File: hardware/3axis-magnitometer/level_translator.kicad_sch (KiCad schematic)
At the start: 10 parts, among them Q1 BSS138, Q2 BSS138

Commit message: Add files via upload
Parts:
- removed Q1, Q2: BSS138, Package_TO_SOT_SMD:SOT-23, symbol Transistor_FET:BSS138
- removed R20, R21, R24, R25: 2.2k, Resistor_SMD:R_0805_2012Metric, symbol Device:R
- removed R22, R23: 0, Resistor_SMD:R_0805_2012Metric, symbol Device:R
- added C28, C29, C30, C31, C34, C35: 0.22, Capacitor_SMD:C_0805_2012Metric, symbol Device:C
- added U10, U11: SP3485CN, Package_SO:SOIC-8_3.9x4.9mm_P1.27mm, symbol Interface_UART:SP3485CN
- added U7, U8: 74LVC2T45DC, Package_SO:VSSOP-8_2.3x2mm_P0.5mm, symbol Logic_LevelTranslator:74LVC2T45DC
- renumbered R19 to R14, R26 to R15
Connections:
- net at R15.1: now also C30.1, C31.1, C34.1, C35.1, U10.8 (VCC), U11.8 (VCC), U7.8 (VCCB), U8.8 (VCCB)
- net at R14.2: now also C28.1, C29.1, U7.1 (VCCA), U8.1 (VCCA), U8.5 (DIR)
- new net 485_1_A: U10.6 (A)
- new net 485_1_B: U10.7 (B)
- new net 485_2_A: U11.6 (A)
- new net 485_2_B: U11.7 (B)
- new net GND: C28.2, C29.2, C30.2, C31.2, C34.2, C35.2, U10.5 (GND), U11.5 (GND), U7.4 (GND), U7.5 (DIR), U8.4 (GND)
- new net RX0: U8.2 (1A)
- new net RX1: U8.3 (2A)
- new net TX0: U7.2 (1A)
- new net TX1: U7.3 (2A)
- new net UART_RX0: U10.1 (RO), U8.7 (1B)
- new net UART_RX1: U11.1 (RO), U8.6 (2B)
- new net UART_TX0: U10.4 (DI), U7.7 (1B)
- new net UART_TX1: U11.4 (DI), U7.6 (2B)
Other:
- moved on the sheet: R14, R15

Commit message: начата новая трассировка
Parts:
- added JP1, JP2, JP3, JP4: SolderJumper_2_Open, Jumper:SolderJumper-2_P1.3mm_Open_TrianglePad1.0x1.5mm, symbol Jumper:SolderJumper_2_Open
- added JP5, JP6, JP7, JP8: SolderJumper_3_Open, Jumper:SolderJumper-3_P2.0mm_Open_TrianglePad1.0x1.5mm_NumberLabels, symbol Jumper:SolderJumper_3_Open
- added R15, R16: 2.2k, Resistor_SMD:R_0805_2012Metric, symbol Device:R
- renumbered C28 to C29, C29 to C30, C30 to C32, C34 to C33, C35 to C34, R15 to R17, U11 to U10, U10 to U9
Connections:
- net RX0: now also JP2.1 (A)
- net RX1: now also JP4.1 (A)
- net TX0: now also JP1.1 (A)
- net TX1: now also JP3.1 (A)
- net UART_RX0: now also JP7.2 (C); no longer U8.7 (1B), U9.1 (RO)
- net UART_RX1: now also JP8.2 (C); no longer U10.1 (RO), U8.6 (2B)
- net UART_TX0: now also JP5.2 (C); no longer U7.7 (1B), U9.4 (DI)
- net UART_TX1: now also JP6.2 (C); no longer U10.4 (DI), U7.6 (2B)
- net at C31.1, C32.1, C33.1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: now also R15.1, R16.1
- net at U9.2 (~{RE}): now also U9.3 (DE), R15.2
- net at U10.2 (~{RE}): now also U10.3 (DE), R16.2
- new net: JP3.2 (B), JP6.3 (B), U7.6 (2B)
- new net: JP1.2 (B), JP5.3 (B), U7.7 (1B)
- new net: JP6.1 (A), U10.4 (DI)
- new net: JP7.1 (A), U9.1 (RO)
- new net: JP2.2 (B), JP7.3 (B), U8.7 (1B)
- new net: JP4.2 (B), JP8.3 (B), U8.6 (2B)
- new net: JP5.1 (A), U9.4 (DI)
- new net: JP8.1 (A), U10.1 (RO)
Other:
- moved on the sheet: C29, C30, C31, C32, C33, C34, R17, U10, U7, U8, U9

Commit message: трасировка магнитометра
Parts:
- JP1, JP2, JP3, JP4: footprint Jumper:SolderJumper-2_P1.3mm_Open_TrianglePad1.0x1.5mm -> Jumper:SolderJumper-2_P1.3mm_Open_Pad1.0x1.5mm
- JP5, JP6, JP7, JP8: footprint Jumper:SolderJumper-3_P2.0mm_Open_TrianglePad1.0x1.5mm_NumberLabels -> Jumper:SolderJumper-3_P1.3mm_Open_Pad1.0x1.5mm
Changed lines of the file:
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@@
 			)
 		)
-		(property "Footprint" "Jumper:SolderJumper-3_P2.0mm_Open_TrianglePad1.0x1.5mm_NumberLabels"
+		(property "Footprint" "Jumper:SolderJumper-3_P1.3mm_Open_Pad1.0x1.5mm"
 			(at 137.16 68.58 0)
 			(effects
@@
 			)
 		)
-		(property "Footprint" "Jumper:SolderJumper-3_P2.0mm_Open_TrianglePad1.0x1.5mm_NumberLabels"
+		(property "Footprint" "Jumper:SolderJumper-3_P1.3mm_Open_Pad1.0x1.5mm"
 			(at 144.78 92.71 0)
 			(effects
@@
 			)
 		)
-		(property "Footprint" "Jumper:SolderJumper-2_P1.3mm_Open_TrianglePad1.0x1.5mm"
+		(property "Footprint" "Jumper:SolderJumper-2_P1.3mm_Open_Pad1.0x1.5mm"
 			(at 93.98 25.4 0)
 			(effects
@@
 			)
 		)
-		(property "Footprint" "Jumper:SolderJumper-2_P1.3mm_Open_TrianglePad1.0x1.5mm"
+		(property "Footprint" "Jumper:SolderJumper-2_P1.3mm_Open_Pad1.0x1.5mm"
 			(at 93.98 63.5 0)
 			(effects
@@
 			)
 		)
-		(property "Footprint" "Jumper:SolderJumper-2_P1.3mm_Open_TrianglePad1.0x1.5mm"
+		(property "Footprint" "Jumper:SolderJumper-2_P1.3mm_Open_Pad1.0x1.5mm"
 			(at 88.9 59.69 0)
 			(effects
@@
 			)
 		)
-		(property "Footprint" "Jumper:SolderJumper-2_P1.3mm_Open_TrianglePad1.0x1.5mm"
+		(property "Footprint" "Jumper:SolderJumper-2_P1.3mm_Open_Pad1.0x1.5mm"
 			(at 88.9 21.59 0)
 			(effects
@@
 			)
 		)
-		(property "Footprint" "Jumper:SolderJumper-3_P2.0mm_Open_TrianglePad1.0x1.5mm_NumberLabels"
+		(property "Footprint" "Jumper:SolderJumper-3_P1.3mm_Open_Pad1.0x1.5mm"
 			(at 130.81 54.61 0)
 			(effects
@@
 			)
 		)
-		(property "Footprint" "Jumper:SolderJumper-3_P2.0mm_Open_TrianglePad1.0x1.5mm_NumberLabels"
+		(property "Footprint" "Jumper:SolderJumper-3_P1.3mm_Open_Pad1.0x1.5mm"
 			(at 152.4 106.68 0)
 			(effects

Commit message: Финальные правки трассировки
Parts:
- renumbered C29 to C30, C30 to C31, C31 to C32, C32 to C33, C33 to C34, C34 to C35
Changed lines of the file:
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@@
 		(on_board yes)
 		(dnp no)
-		(property "Reference" "C33"
+		(property "Reference" "C34"
 			(at 116.84 110.236 0)
 			(effects
@@
 			(project "3axis-magnitometer"
 				(path "/c590c88d-27c9-4e5a-a435-a42d9de70c1c/83e74227-fab1-47ae-b3ea-3e1f54a43bc9"
-					(reference "C33")
+					(reference "C34")
 					(unit 1)
 				)
@@
 		(on_board yes)
 		(dnp no)
-		(property "Reference" "C29"
+		(property "Reference" "C30"
 			(at 78.74 36.576 0)
 			(effects
@@
 			(project "3axis-magnitometer"
 				(path "/c590c88d-27c9-4e5a-a435-a42d9de70c1c/83e74227-fab1-47ae-b3ea-3e1f54a43bc9"
-					(reference "C29")
+					(reference "C30")
 					(unit 1)
 				)
@@
 		(on_board yes)
 		(dnp no)
-		(property "Reference" "C32"
+		(property "Reference" "C33"
 			(at 116.84 93.726 0)
 			(effects
@@
 			(project "3axis-magnitometer"
 				(path "/c590c88d-27c9-4e5a-a435-a42d9de70c1c/83e74227-fab1-47ae-b3ea-3e1f54a43bc9"
-					(reference "C32")
+					(reference "C33")
 					(unit 1)
 				)
@@
 		(on_board yes)
 		(dnp no)
-		(property "Reference" "C30"
+		(property "Reference" "C31"
 			(at 78.74 94.996 0)
 			(effects
@@
 			(project "3axis-magnitometer"
 				(path "/c590c88d-27c9-4e5a-a435-a42d9de70c1c/83e74227-fab1-47ae-b3ea-3e1f54a43bc9"
-					(reference "C30")
+					(reference "C31")
 					(unit 1)
 				)
@@
 		(on_board yes)
 		(dnp no)
-		(property "Reference" "C31"
+		(property "Reference" "C32"
 			(at 116.84 51.816 0)
 			(effects
@@
 			(project "3axis-magnitometer"
 				(path "/c590c88d-27c9-4e5a-a435-a42d9de70c1c/83e74227-fab1-47ae-b3ea-3e1f54a43bc9"
-					(reference "C31")
+					(reference "C32")
 					(unit 1)
 				)
@@
 		(on_board yes)
 		(dnp no)
-		(property "Reference" "C34"
+		(property "Reference" "C35"
 			(at 116.84 148.336 0)
 			(effects
@@
 			(project "3axis-magnitometer"
 				(path "/c590c88d-27c9-4e5a-a435-a42d9de70c1c/83e74227-fab1-47ae-b3ea-3e1f54a43bc9"
-					(reference "C34")
-					(unit 1)
-				)
+					(reference "C35")
+					(unit 1)
+				)

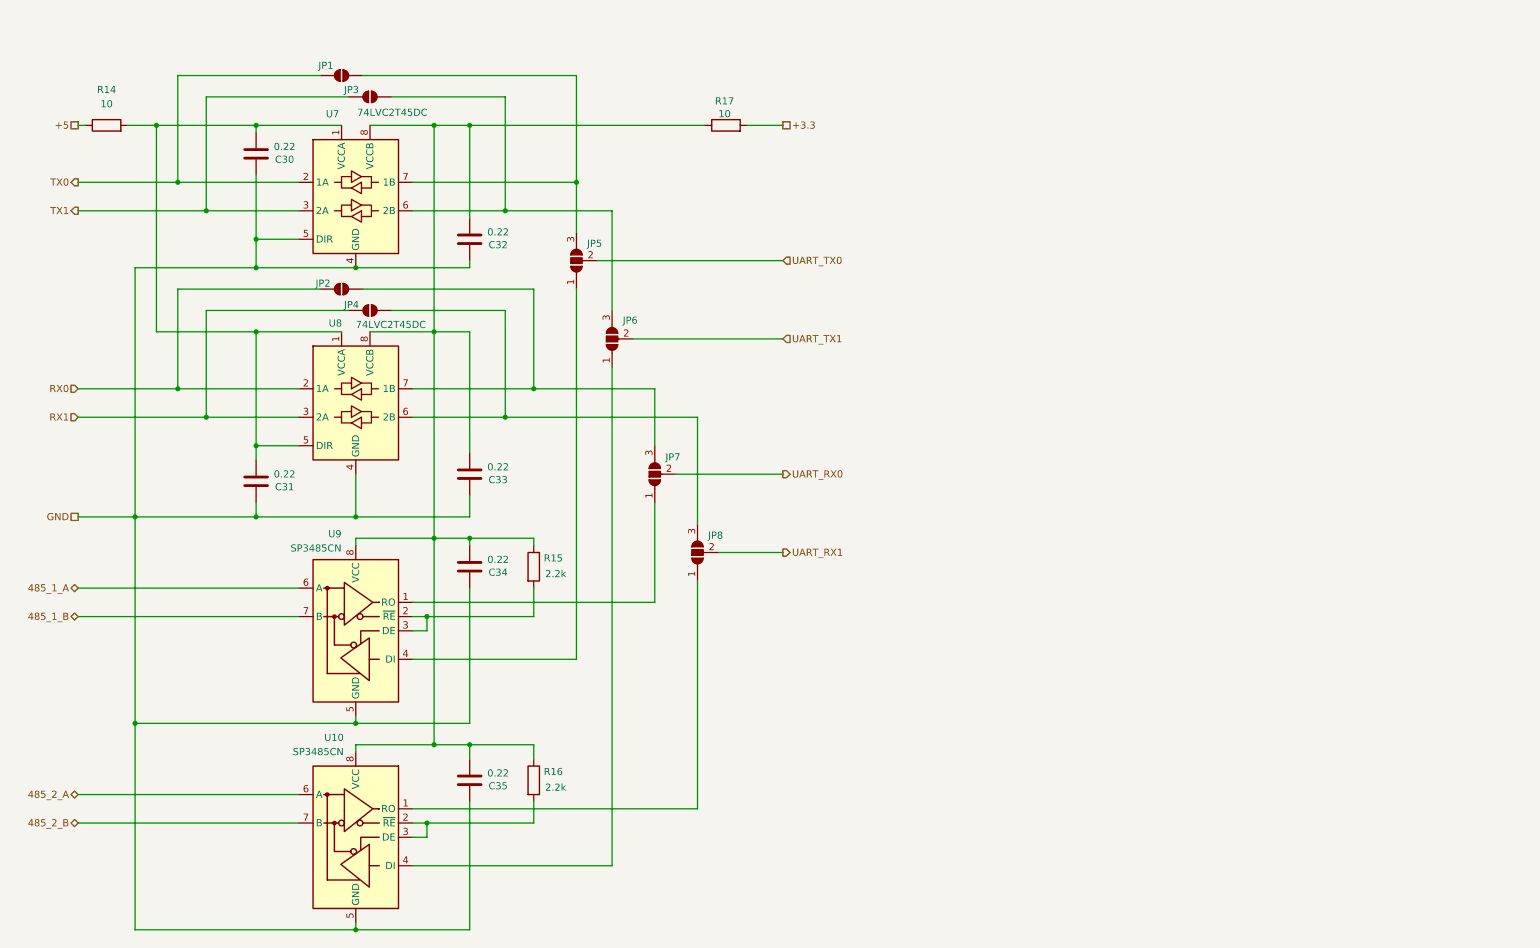
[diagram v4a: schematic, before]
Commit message: замена микросхемы преобразователя  уровня
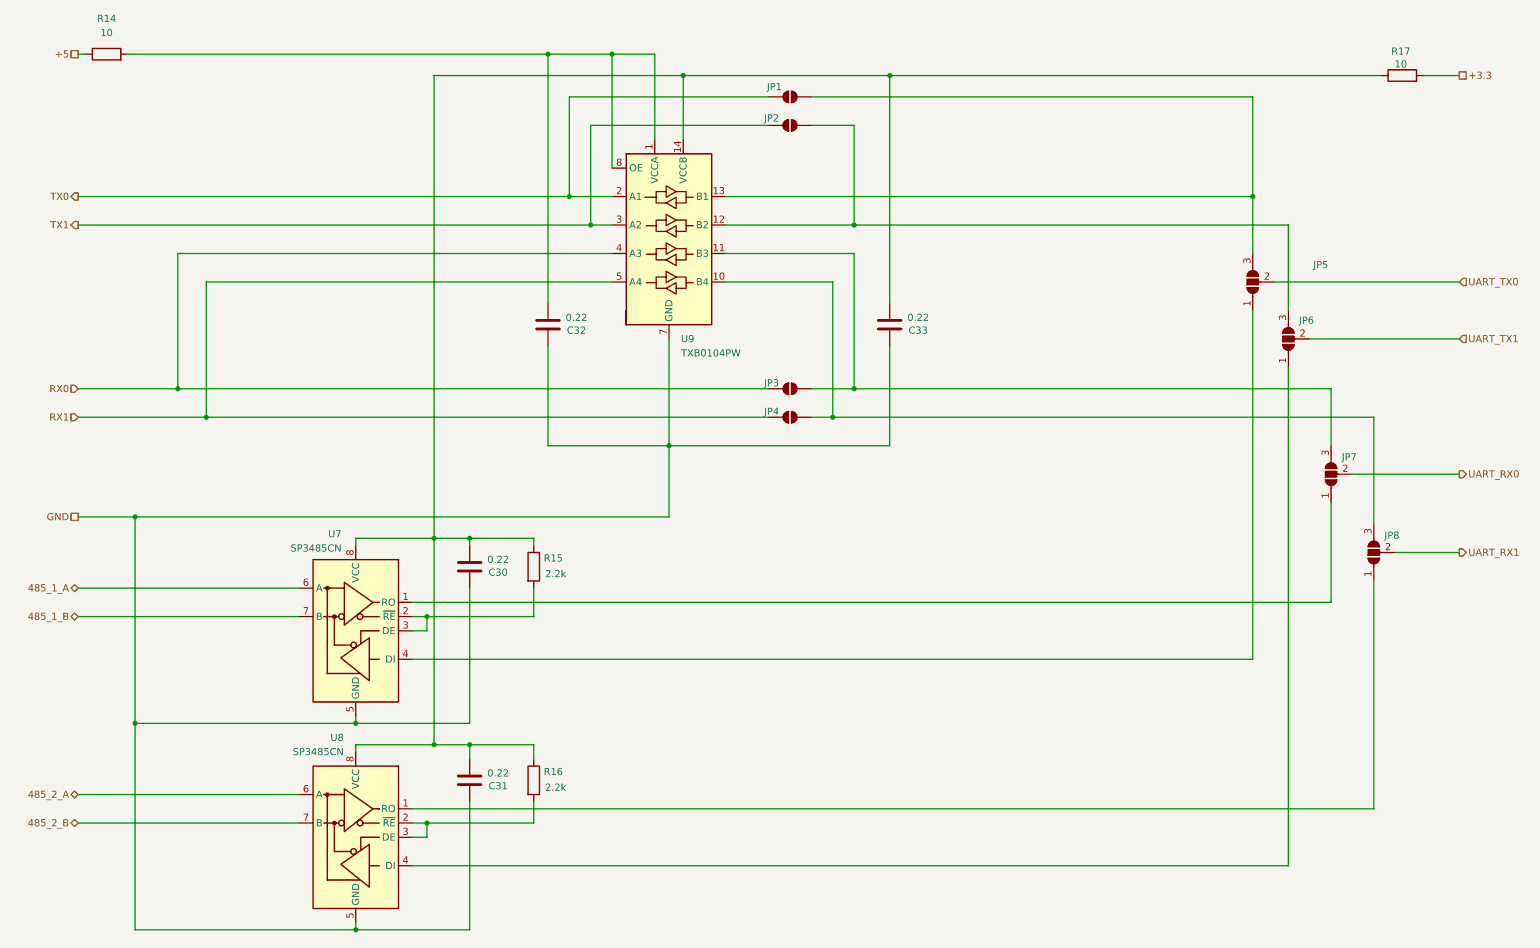
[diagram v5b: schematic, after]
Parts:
- removed C31, C33: 0.22, Capacitor_SMD:C_0805_2012Metric, symbol Device:C
- removed U7, U8: 74LVC2T45DC, Package_SO:VSSOP-8_2.3x2mm_P0.5mm, symbol Logic_LevelTranslator:74LVC2T45DC
- added U9: TXB0104PW, Package_SO:TSSOP-14_4.4x5mm_P0.65mm, symbol Logic_LevelTranslator:TXB0104PW
- renumbered C34 to C30, C35 to C31, C30 to C32, C32 to C33, JP3 to JP2, JP2 to JP3, U9 to U7, U10 to U8
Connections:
- net GND: now also U9.7 (GND)
- net RX0: now also U9.4 (A3)
- net RX1: now also U9.5 (A4)
- net TX0: now also U9.2 (A1)
- net TX1: now also U9.3 (A2)
- net at C32.1, R14.2: now also U9.1 (VCCA), U9.8 (OE)
- net at JP2.2 (B), JP6.3 (B): now also U9.12 (B2)
- net at JP1.2 (B), JP5.3 (B): now also U9.13 (B1)
- net at C30.1, C31.1, C33.1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: now also U9.14 (VCCB)
- net at JP3.2 (B), JP7.3 (B): now also U9.11 (B3)
- net at JP4.2 (B), JP8.3 (B): now also U9.10 (B4)
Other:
- moved on the sheet: C32, C33, JP1, JP2, JP3, JP4, JP5, JP6, JP7, JP8, R14, R17
